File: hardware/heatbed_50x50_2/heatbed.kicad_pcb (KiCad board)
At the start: 2 copper layers, 50 x 50 mm, 1 part, among them J1 PWR

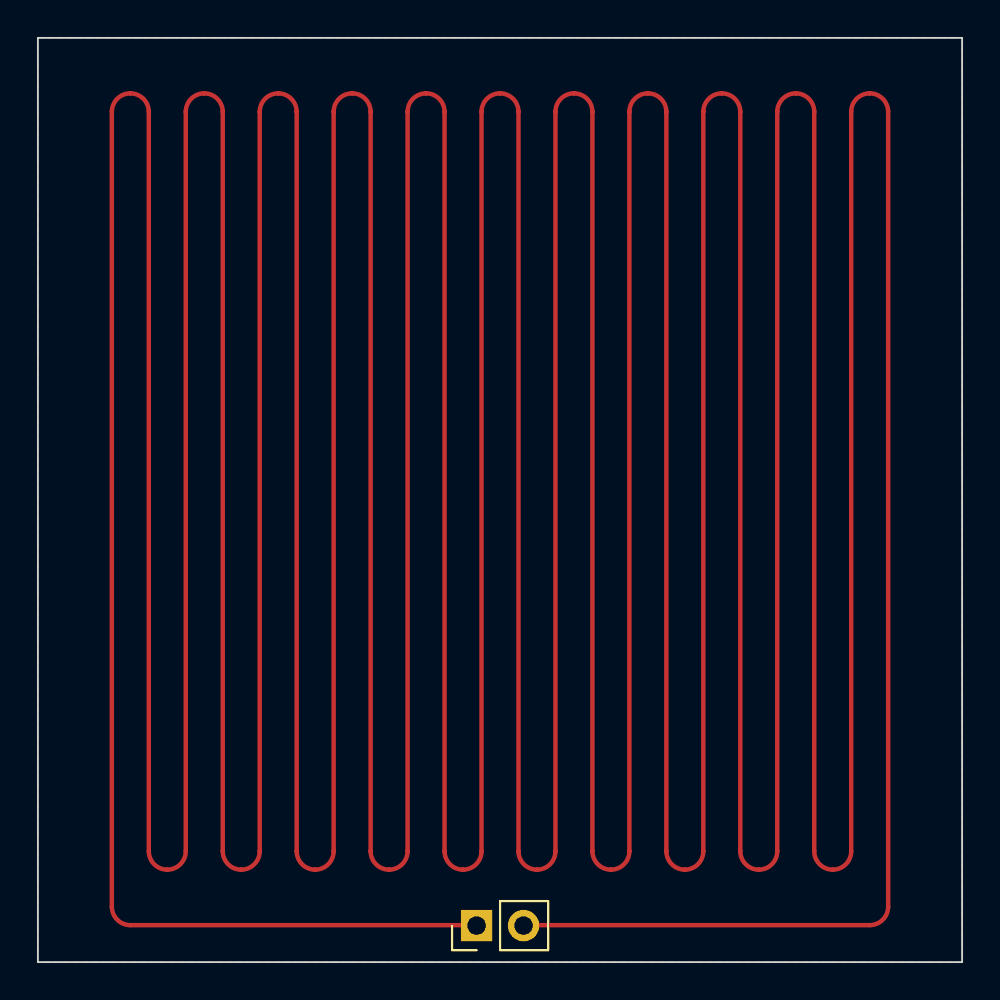
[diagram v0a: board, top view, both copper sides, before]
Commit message: Further increase tracks' widths
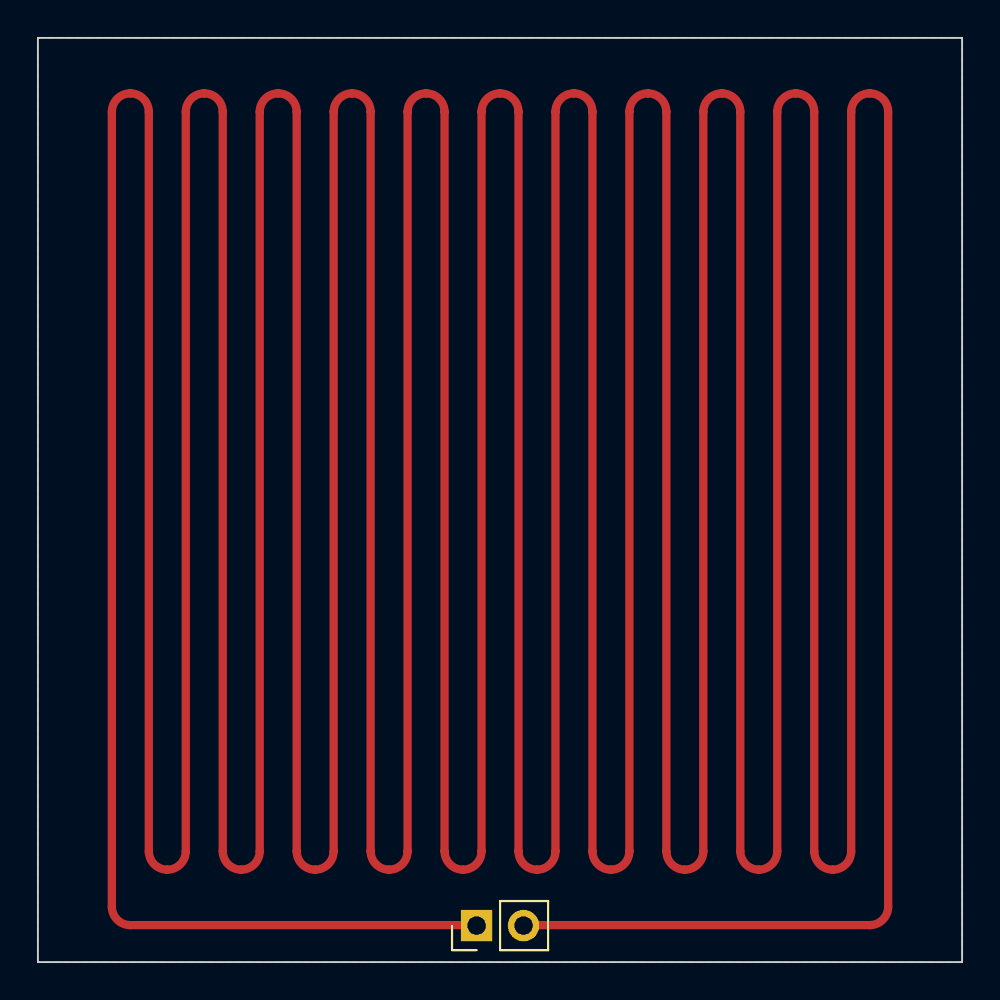
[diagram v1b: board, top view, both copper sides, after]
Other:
- board text added: "Width: 0.449 mm | Length: 992.64 mm | Resistance: 1.91 Ω"
- board text removed: "Width: 0.241 mm | Length: 992.64 mm | Resistance: 3.37 Ω"

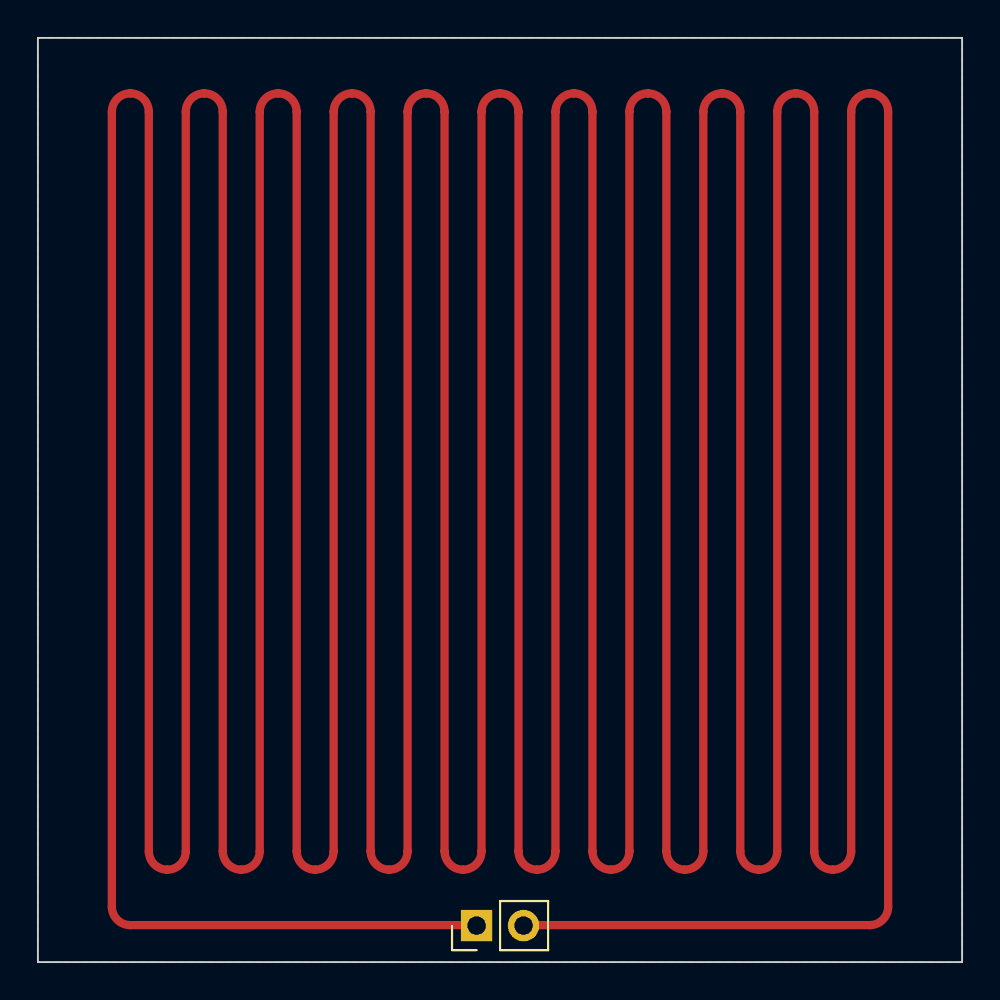
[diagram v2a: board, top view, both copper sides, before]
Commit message: Increase holes' diameters
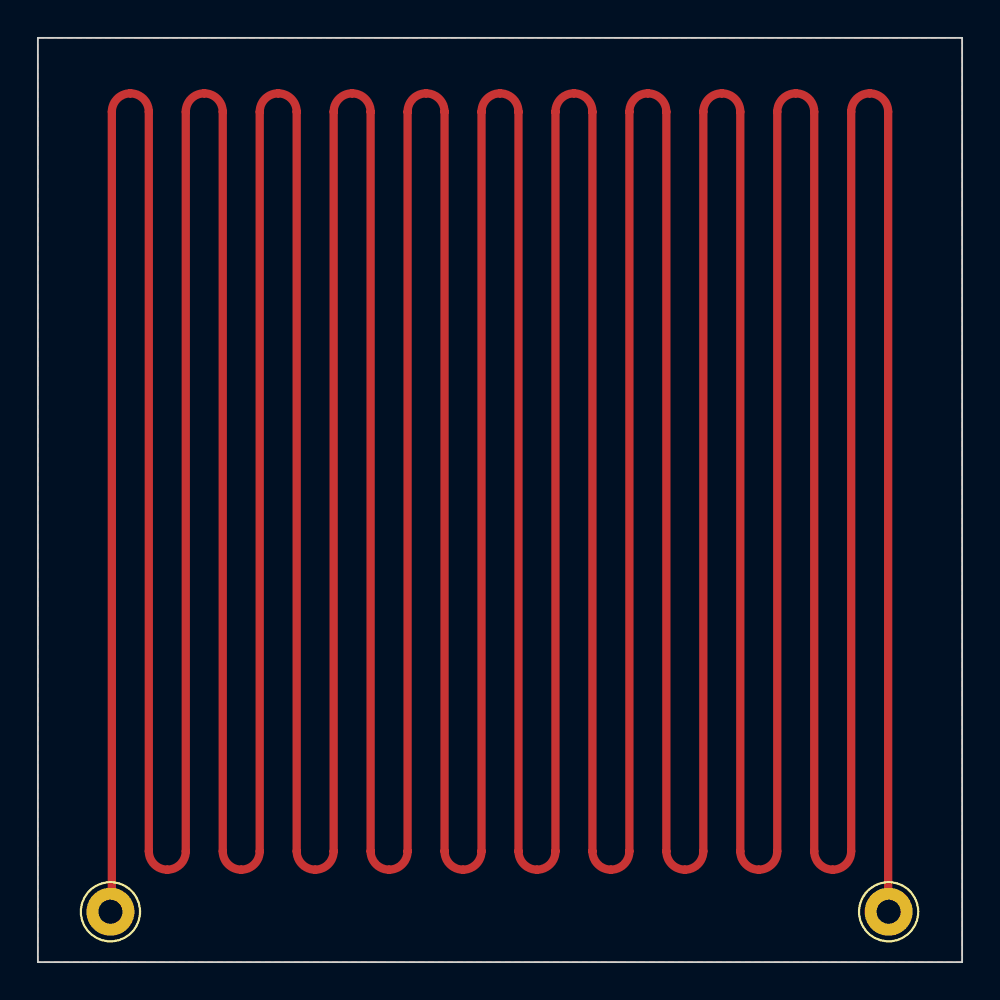
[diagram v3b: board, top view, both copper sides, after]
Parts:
- added J2: Conn_01x01, Connector_Pin:Pin_D1.3mm_L11.0mm, F.Cu at (167.0, 126.3)
- J1: value PWR -> Conn_01x01; footprint Connector_PinHeader_2.54mm:PinHeader_1x02_P2.54mm_Vertical -> Connector_Pin:Pin_D1.3mm_L11.0mm
- moved J1 19.8 mm to (124.9, 126.3), turned to 0 degrees
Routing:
- net Net-(J1-Pin_1): track 990.8 -> 950.9 mm
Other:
- board text removed: "Width: 0.449 mm | Length: 992.64 mm | Resistance: 1.91 Ω"
